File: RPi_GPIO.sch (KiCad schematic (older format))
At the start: 42 parts, among them J2 RPi_GPIO, J3 Conn_02x03_Counter_Clockwise, J5 Conn_01x03_Male, J6 Conn_01x03_Male, J7 Conn_01x03_Male, J8 Conn_01x03_Male, J9 Conn_01x03_Male, SW1 SW_Push, U2 STM32F030CCTx, U3 MAX485E, U4 MAX485E, U5 MAX485E, U6 MAX485E, U7 MAX485E

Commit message: Finished routing
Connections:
- no-connect marks 50 -> 51
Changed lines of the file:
@@
 Text Label 3750 5500 2    50   ~ 0
 PA8
+NoConn ~ 1700 4700
 $EndSCHEMATC

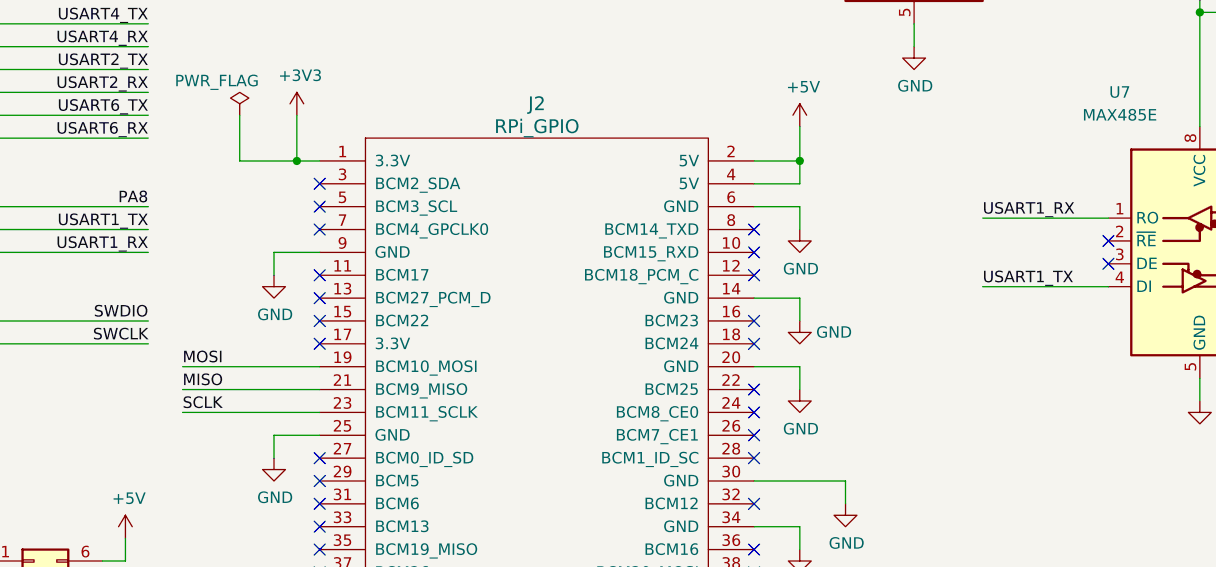
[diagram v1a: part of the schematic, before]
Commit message: Connect reset and boot0 to raspi and change few things
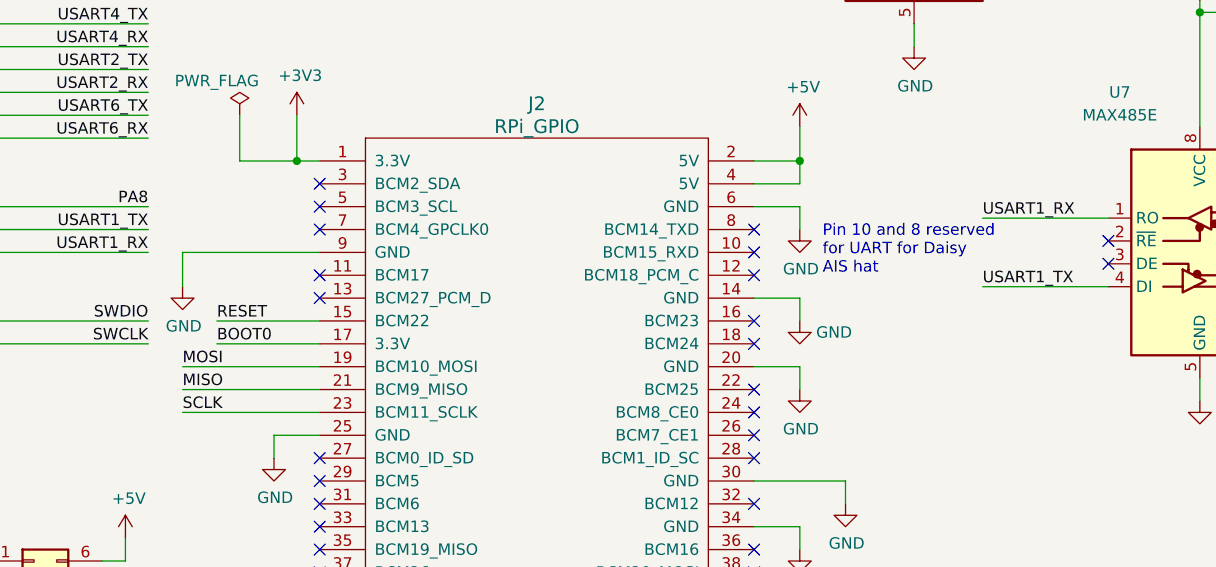
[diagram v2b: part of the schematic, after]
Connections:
- net BOOT0: now also J2.17 (3.3V)
- net RESET: now also J2.15 (BCM22)
- no-connect marks 51 -> 49
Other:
- note added: "Pin 10 and 8 reserved \nfor UART for Daisy \nAIS hat"
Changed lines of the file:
@@
 	1    0    0    -1
 $EndComp
-Wire Wire Line
-	4500 5700 4300 5700
-Wire Wire Line
-	4300 5700 4300 5800
 $Comp
 L power:GND #PWR?
 U 1 1 5C4D2E71
-P 4300 5800
-F 0 "#PWR?" H 4300 5550 50  0001 C CNN
-F 1 "GND" H 4305 5627 50  0000 C CNN
-F 2 "" H 4300 5800 50  0001 C CNN
-F 3 "" H 4300 5800 50  0001 C CNN
-	1    4300 5800
+P 3900 5850
+F 0 "#PWR?" H 3900 5600 50  0001 C CNN
+F 1 "GND" H 3905 5677 50  0000 C CNN
+F 2 "" H 3900 5850 50  0001 C CNN
+F 3 "" H 3900 5850 50  0001 C CNN
+	1    3900 5850
 	1    0    0    -1
 $EndComp
@@
 NoConn ~ 4500 6700
 NoConn ~ 4500 6600
-NoConn ~ 4500 6100
-NoConn ~ 4500 6000
 NoConn ~ 4500 5900
 NoConn ~ 4500 5800
@@
 PA8
 NoConn ~ 1700 4700
+Text Notes 6700 5800 0    50   ~ 0
+Pin 10 and 8 reserved \nfor UART for Daisy \nAIS hat
+Wire Wire Line
+	3900 5700 3900 5850
+Wire Wire Line
+	3900 5700 4500 5700
+Wire Wire Line
+	4500 6100 4050 6100
+Wire Wire Line
+	4500 6000 4050 6000
+Text Label 4050 6000 0    50   ~ 0
+RESET
+Text Label 4050 6100 0    50   ~ 0
+BOOT0
 $EndSCHEMATC

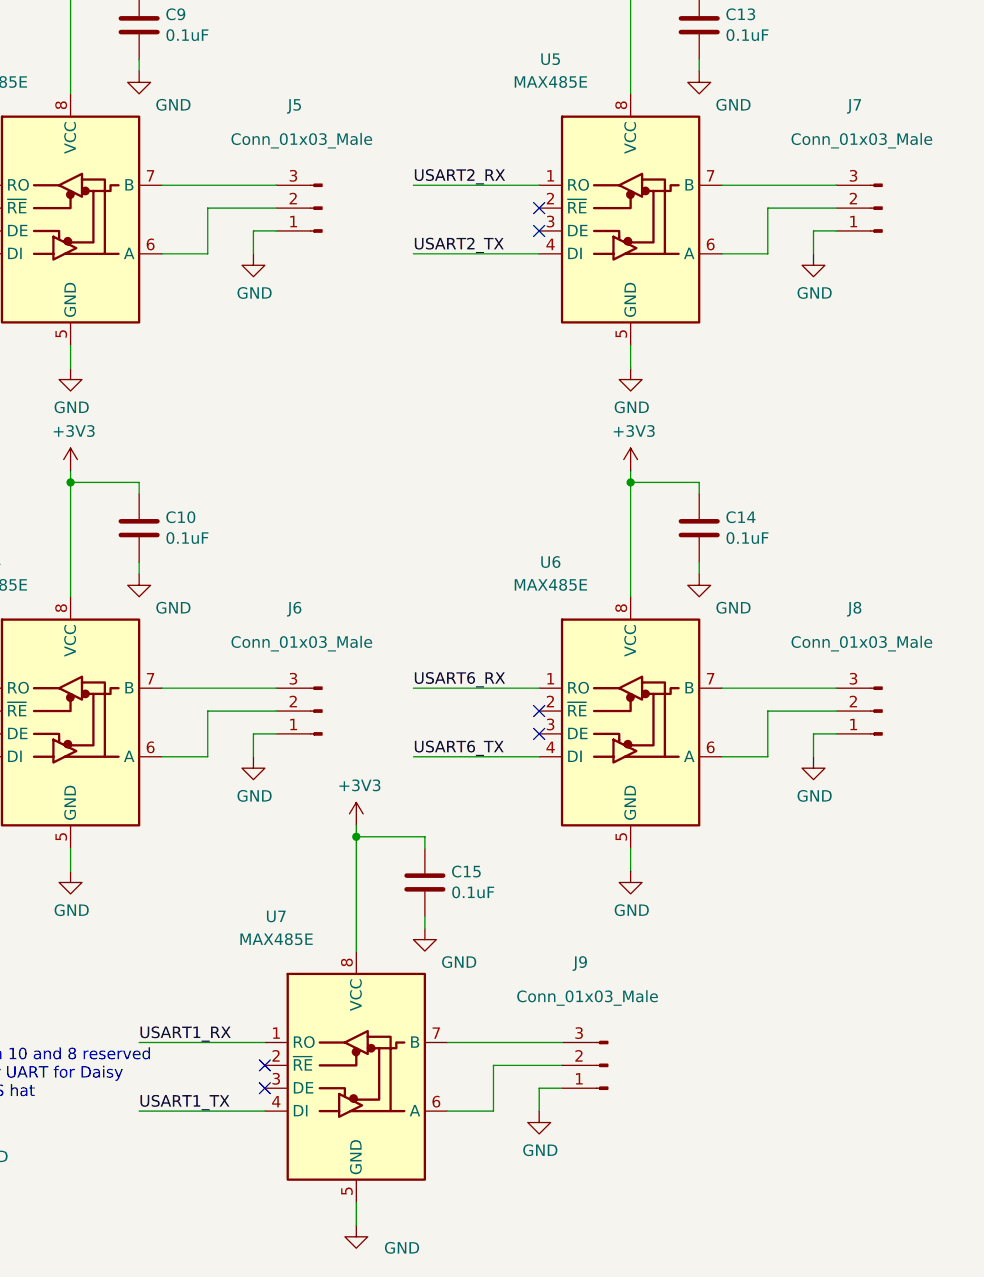
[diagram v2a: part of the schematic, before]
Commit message: Add termination resistors in schematics
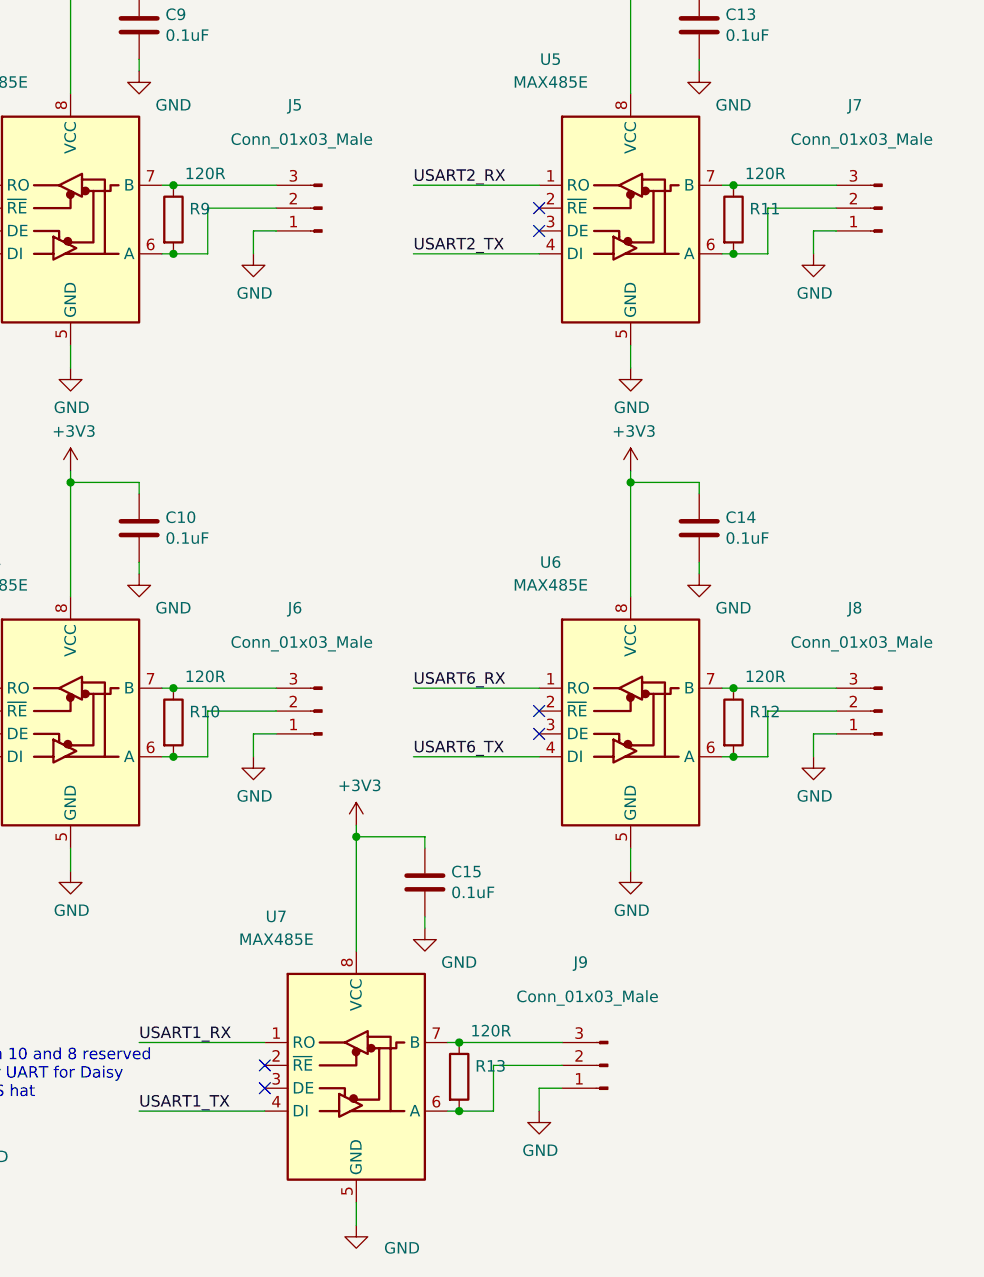
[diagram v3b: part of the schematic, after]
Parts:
- added R10, R11, R12, R13, R9: 120R, Resistors_SMD:R_0603_HandSoldering, symbol Device:R
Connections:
- net at J5.2 (Pin_2), U3.6 (A): now also R9.2
- net at J5.3 (Pin_3), U3.7 (B): now also R9.1
- net at J7.2 (Pin_2), U5.6 (A): now also R11.2
- net at J7.3 (Pin_3), U5.7 (B): now also R11.1
- net at J6.2 (Pin_2), U4.6 (A): now also R10.2
- net at J6.3 (Pin_3), U4.7 (B): now also R10.1
- net at J8.2 (Pin_2), U6.6 (A): now also R12.2
- net at J8.3 (Pin_3), U6.7 (B): now also R12.1
- net at J9.2 (Pin_2), U7.6 (A): now also R13.2
- net at J9.3 (Pin_3), U7.7 (B): now also R13.1
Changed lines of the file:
@@
 $EndComp
 Wire Wire Line
-	7700 2100 7500 2100
-Wire Wire Line
-	7500 1800 8000 1800
+	7700 2100 7550 2100
+Wire Wire Line
+	7500 1800 7550 1800
 $Comp
 L Interface_UART:MAX485E U5
@@
 $EndComp
 Wire Wire Line
-	10150 2100 9950 2100
-Wire Wire Line
-	9950 1800 10450 1800
+	10150 2100 10000 2100
+Wire Wire Line
+	9950 1800 10000 1800
 $Comp
 L Interface_UART:MAX485E U4
@@
 $EndComp
 Wire Wire Line
-	7700 4300 7500 4300
-Wire Wire Line
-	7500 4000 8000 4000
+	7700 4300 7550 4300
+Wire Wire Line
+	7500 4000 7550 4000
 $Comp
 L Interface_UART:MAX485E U6
@@
 $EndComp
 Wire Wire Line
-	10150 4300 9950 4300
-Wire Wire Line
-	9950 4000 10450 4000
+	10150 4300 10000 4300
+Wire Wire Line
+	9950 4000 10000 4000
 Wire Wire Line
 	3000 6000 3750 6000
@@
 $EndComp
 Wire Wire Line
-	8950 5850 8750 5850
-Wire Wire Line
-	8750 5550 9250 5550
+	8950 5850 8800 5850
+Wire Wire Line
+	8750 5550 8800 5550
 NoConn ~ 7950 5650
 NoConn ~ 7950 5750
@@
 Text Label 4050 6100 0    50   ~ 0
 BOOT0
+$Comp
+L Device:R R10
+U 1 1 5C6B9F5C
+P 7550 4150
+F 0 "R10" H 7620 4196 50  0000 L CNN
+F 1 "120R" H 7600 4350 50  0000 L CNN
+F 2 "Resistors_SMD:R_0603_HandSoldering" V 7480 4150 50  0001 C CNN
+F 3 "~" H 7550 4150 50  0001 C CNN
+	1    7550 4150
+	1    0    0    -1
+$EndComp
+Connection ~ 7550 4000
+Wire Wire Line
+	7550 4000 8000 4000
+Connection ~ 7550 4300
+Wire Wire Line
+	7550 4300 7500 4300
+$Comp
+L Device:R R12
+U 1 1 5C6BB9D4
+P 10000 4150
+F 0 "R12" H 10070 4196 50  0000 L CNN
+F 1 "120R" H 10050 4350 50  0000 L CNN
+F 2 "Resistors_SMD:R_0603_HandSoldering" V 9930 4150 50  0001 C CNN
+F 3 "~" H 10000 4150 50  0001 C CNN
+	1    10000 4150
+	1    0    0    -1
+$EndComp
+Connection ~ 10000 4000
+Wire Wire Line
+	10000 4000 10450 4000
+Connection ~ 10000 4300
+Wire Wire Line
+	10000 4300 9950 4300
+$Comp
+L Device:R R9
+U 1 1 5C6BC45A
+P 7550 1950
+F 0 "R9" H 7620 1996 50  0000 L CNN
+F 1 "120R" H 7600 2150 50  0000 L CNN
+F 2 "Resistors_SMD:R_0603_HandSoldering" V 7480 1950 50  0001 C CNN
+F 3 "~" H 7550 1950 50  0001 C CNN
+	1    7550 1950
+	1    0    0    -1
+$EndComp
+Connection ~ 7550 1800
+Wire Wire Line
+	7550 1800 8000 1800
+Connection ~ 7550 2100
+Wire Wire Line
+	7550 2100 7500 2100
+$Comp
+L Device:R R11
+U 1 1 5C6BCADA
+P 10000 1950
+F 0 "R11" H 10070 1996 50  0000 L CNN
+F 1 "120R" H 10050 2150 50  0000 L CNN
+F 2 "Resistors_SMD:R_0603_HandSoldering" V 9930 1950 50  0001 C CNN
+F 3 "~" H 10000 1950 50  0001 C CNN
+	1    10000 1950
+	1    0    0    -1
+$EndComp
+Connection ~ 10000 1800
+Wire Wire Line
+	10000 1800 10450 1800
+Connection ~ 10000 2100
+Wire Wire Line
+	10000 2100 9950 2100
+$Comp
+L Device:R R13
+U 1 1 5C6BDB0E
+P 8800 5700
+F 0 "R13" H 8870 5746 50  0000 L CNN
+F 1 "120R" H 8850 5900 50  0000 L CNN
+F 2 "Resistors_SMD:R_0603_HandSoldering" V 8730 5700 50  0001 C CNN
+F 3 "~" H 8800 5700 50  0001 C CNN
+	1    8800 5700
+	1    0    0    -1
+$EndComp
+Connection ~ 8800 5550
+Wire Wire Line
+	8800 5550 9250 5550
+Connection ~ 8800 5850
+Wire Wire Line
+	8800 5850 8750 5850
 $EndSCHEMATC

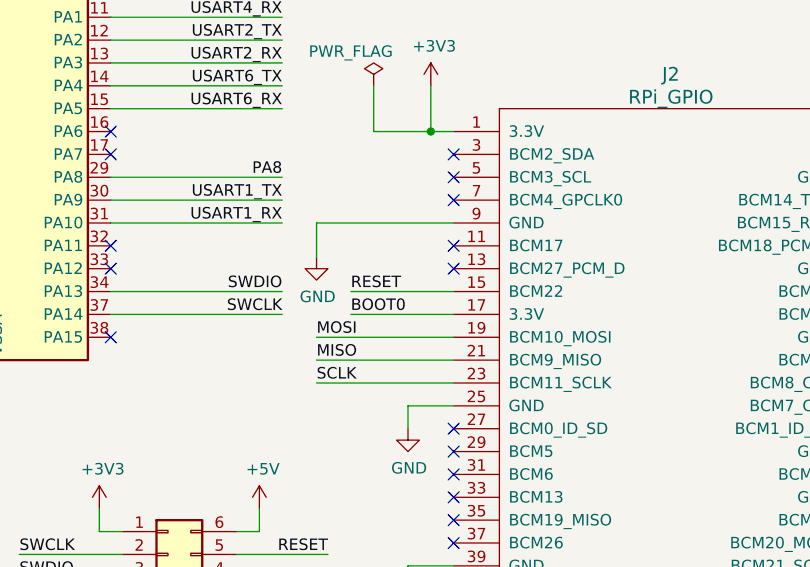
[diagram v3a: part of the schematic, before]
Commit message: Add terminaison resistors
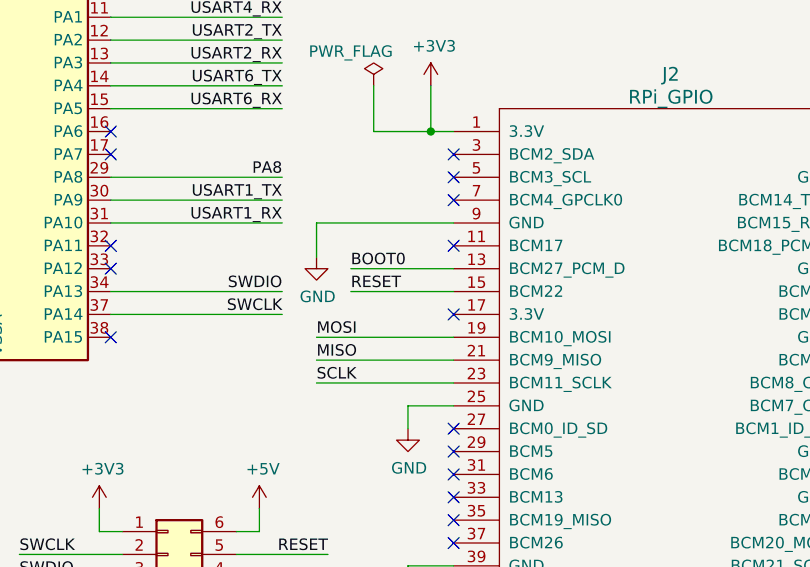
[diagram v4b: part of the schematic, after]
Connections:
- net BOOT0: now also J2.13 (BCM27_PCM_D); no longer J2.17 (3.3V)
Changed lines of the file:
@@
 NoConn ~ 4500 6700
 NoConn ~ 4500 6600
-NoConn ~ 4500 5900
 NoConn ~ 4500 5800
 NoConn ~ 4500 5600
@@
 	3900 5700 4500 5700
 Wire Wire Line
-	4500 6100 4050 6100
+	4500 5900 4050 5900
 Wire Wire Line
 	4500 6000 4050 6000
 Text Label 4050 6000 0    50   ~ 0
 RESET
-Text Label 4050 6100 0    50   ~ 0
+Text Label 4050 5900 0    50   ~ 0
 BOOT0
 $Comp
@@
 Wire Wire Line
 	8800 5850 8750 5850
+NoConn ~ 4500 6100
 $EndSCHEMATC
